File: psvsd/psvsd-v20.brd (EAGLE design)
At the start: 30 x 33.2 mm, 27 parts, among them U1 GL823(A)OG, U2 74AUP1G74DC, U3 LP3996_DSC_10

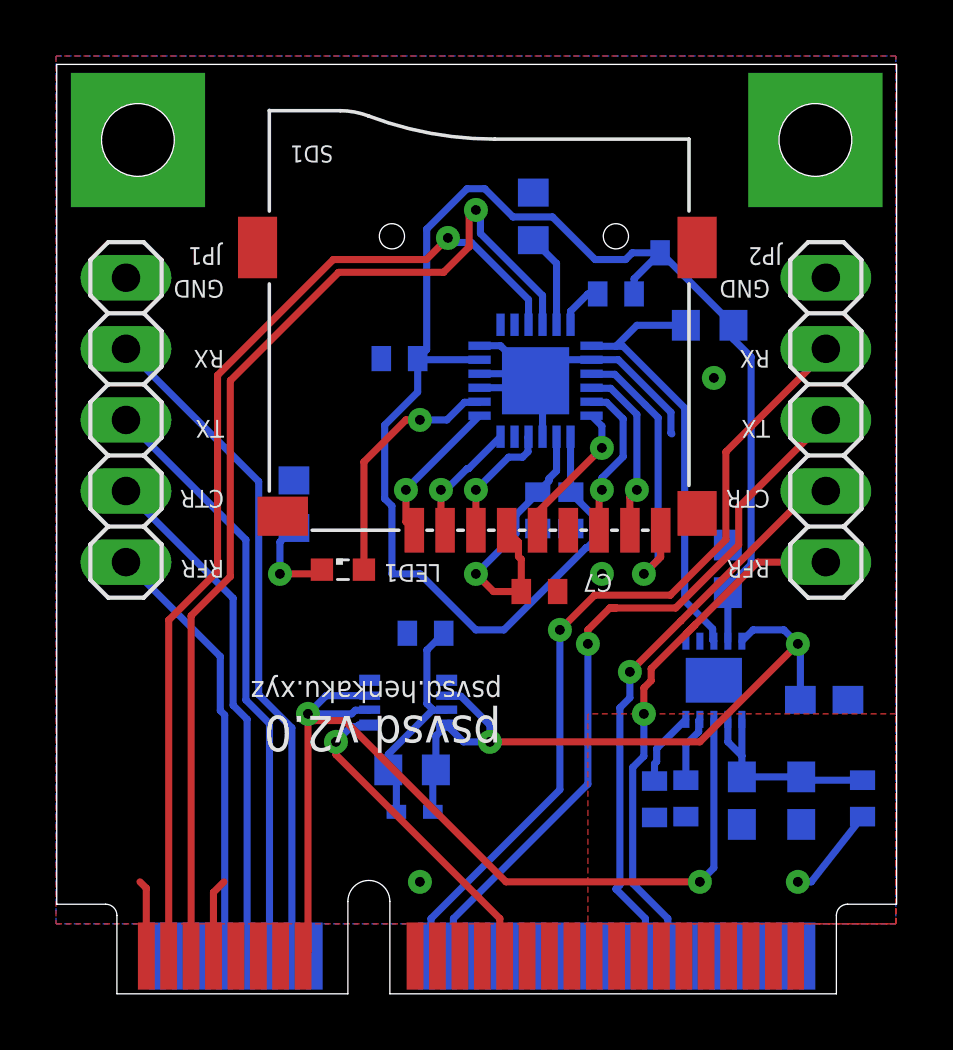
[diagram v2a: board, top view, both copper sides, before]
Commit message: Added RC delay to power circuit
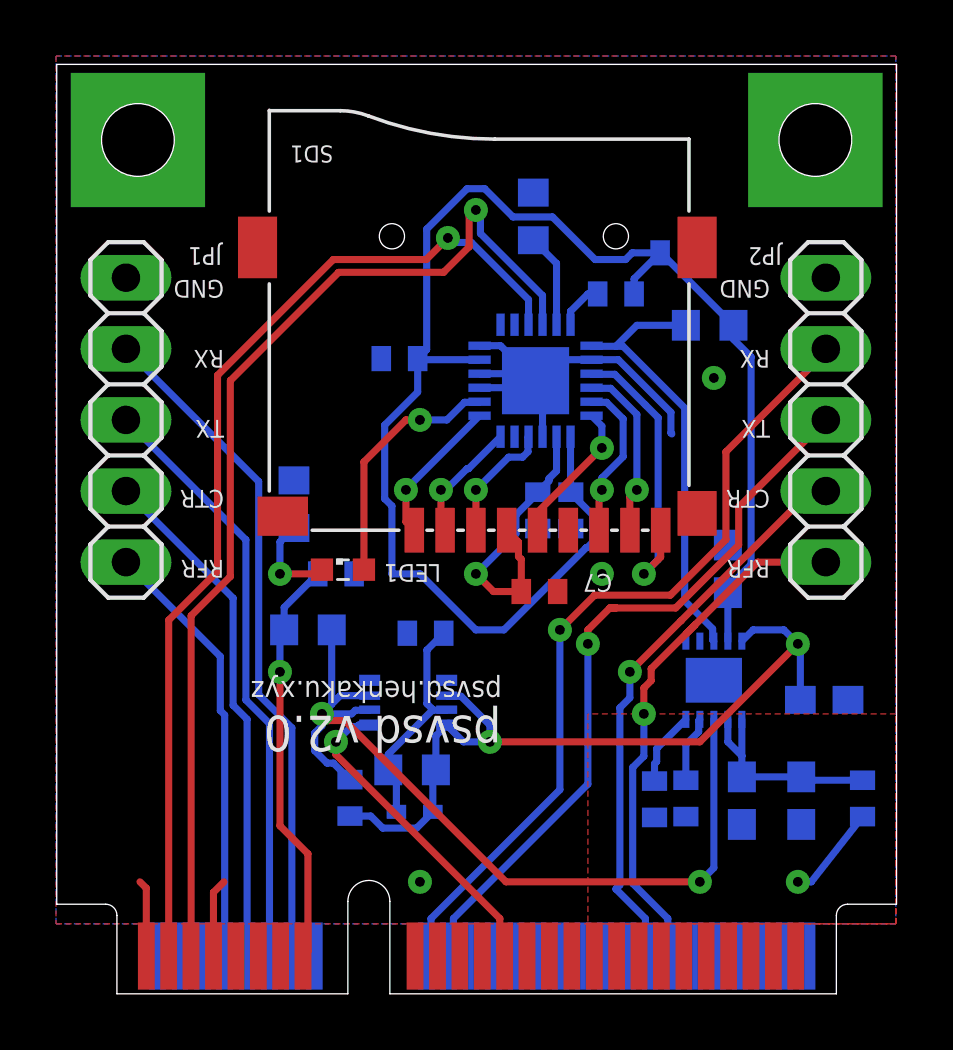
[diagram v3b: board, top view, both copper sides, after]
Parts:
- added C9: (no value), rcl:C0402
- added R4: 0, rcl:R0402
- added R5: (no value), rcl:R0603
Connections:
- new net PWR_ON: R4.2, R5.2, U2.2, U2.3, U3.3
- net GND: now also C9.2
- net PSHOLD: now also C9.1, R5.1; no longer U2.2, U2.3, U3.3
- net VDD18: now also R4.1
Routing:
- net PWR_ON: track 0.00 -> 32.0 mm, vias 0 -> 2
- net PSHOLD: track 36.0 -> 14.9 mm, vias 2 -> 1
- net VDD18: track 24.6 -> 28.0 mm
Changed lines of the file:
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@@
 <element name="SD1" library="Seeed-Connector" library_urn="urn:adsk.eagle:library:478" package="MICRO-SD9+4P-SMD-16.1X14.5X1.85MM" value="ST-TF-003A" x="15.05" y="16.56" smashed="yes" rot="R90">
 <attribute name="MPN" value="ST-TF-003A" x="15.05" y="16.56" size="1.778" layer="27" rot="R90" display="off"/>
+<attribute name="NAME" x="9.9" y="30.303" size="0.6096" layer="25" ratio="11" rot="SR180"/>
 <attribute name="NAME" x="12.891" y="21.386" size="0.254" layer="33" ratio="10" rot="R90"/>
-<attribute name="NAME" x="9.9" y="30.303" size="0.6096" layer="25" ratio="11" rot="SR180"/>
 <attribute name="VALUE" x="18.86" y="19.735" size="0.508" layer="27" ratio="10" rot="SR180"/>
 </element>
@@
 </element>
 <element name="FB2" library="inductors" library_urn="urn:adsk.eagle:library:243" package="0402" value="" x="20" y="25" rot="MR0"/>
+<element name="R4" library="rcl" library_urn="urn:adsk.eagle:library:334" package="R0402" value="0" x="10.5" y="7" rot="MR90"/>
+<element name="C9" library="rcl" library_urn="urn:adsk.eagle:library:334" package="C0402" value="" x="10" y="15" rot="MR180"/>
+<element name="R5" library="rcl" library_urn="urn:adsk.eagle:library:334" package="R0603" value="" x="9" y="13" rot="MR180"/>
 </elements>
 <signals>
@@
 <wire x1="5.626" y1="1.35" x2="5.626" y2="3.626" width="0.254" layer="1"/>
 <wire x1="5.626" y1="3.626" x2="6" y2="4" width="0.254" layer="1"/>
+<contactref element="C9" pad="2"/>
 </signal>
 <signal name="UART_KERMIT_RFR">
@@
 <wire x1="10" y1="9" x2="10" y2="8.542975" width="0.254" layer="1"/>
 <wire x1="10" y1="8.542975" x2="15.8562" y2="2.686775" width="0.254" layer="1"/>
-</signal>
-<signal name="PSHOLD">
-<contactref element="U$1" pad="15"/>
-<contactref element="U2" pad="3"/>
-<contactref element="U2" pad="2"/>
-<contactref element="U3" pad="3"/>
-<via x="23" y="4" extent="1-16" drill="0.35"/>
-<wire x1="23.5" y1="9.803" x2="23.5" y2="4.5" width="0.254" layer="16"/>
-<wire x1="23.5" y1="4.5" x2="23" y2="4" width="0.254" layer="16"/>
-<via x="9" y="10" extent="1-16" drill="0.35"/>
-<wire x1="9" y1="10" x2="9" y2="1.524" width="0.254" layer="1"/>
-<wire x1="9" y1="1.524" x2="8.826" y2="1.35" width="0.254" layer="1"/>
-<wire x1="10.563025" y1="10" x2="9" y2="10" width="0.254" layer="16"/>
-<wire x1="10.563025" y1="10" x2="10.693225" y2="10.1302" width="0.254" layer="16"/>
-<wire x1="10.693225" y1="10.1302" x2="11.1852" y2="10.1302" width="0.254" layer="16"/>
-<wire x1="11.1852" y1="10.1302" x2="11.205" y2="10.15" width="0.254" layer="16"/>
-<wire x1="9" y1="10" x2="9.65" y2="10.65" width="0.254" layer="16"/>
-<wire x1="9.65" y1="10.65" x2="11.205" y2="10.65" width="0.254" layer="16"/>
-<wire x1="9.2408" y1="9.7592" x2="9" y2="10" width="0.254" layer="1"/>
-<wire x1="10.314475" y1="9.7592" x2="9.2408" y2="9.7592" width="0.254" layer="1"/>
-<wire x1="23" y1="4" x2="16.073675" y2="4" width="0.254" layer="1"/>
-<wire x1="16.073675" y1="4" x2="10.314475" y2="9.7592" width="0.254" layer="1"/>
 </signal>
 <signal name="VDD33">
@@
 <contactref element="D1" pad="C"/>
 <contactref element="U2" pad="8"/>
-<wire x1="13.57" y1="9.215" x2="13.955" y2="9.6" width="0.254" layer="16"/>
+<wire x1="13.955" y1="9.6" x2="13.57" y2="9.215" width="0.254" layer="16"/>
 <wire x1="13.57" y1="9.215" x2="13.57" y2="8" width="0.254" layer="16"/>
 <wire x1="13.57" y1="8" x2="13.46" y2="7.89" width="0.254" layer="16"/>
-<wire x1="13.46" y1="7.89" x2="13.46" y2="6.5" width="0.254" layer="16"/>
+<wire x1="13.46" y1="6.5" x2="13.46" y2="7.89" width="0.254" layer="16"/>
 <via x="15.5" y="9" extent="1-16" drill="0.35"/>
 <via x="26.5" y="12.5" extent="1-16" drill="0.35"/>
@@
 <wire x1="26.59" y1="12.41" x2="26.59" y2="10.5" width="0.254" layer="16"/>
 <wire x1="13.955" y1="9.6" x2="14.555" y2="9" width="0.254" layer="16"/>
-<wire x1="14.555" y1="9" x2="15.5" y2="9" width="0.254" layer="16"/>
+<wire x1="15.5" y1="9" x2="14.555" y2="9" width="0.254" layer="16"/>
 <wire x1="13.955" y1="10.65" x2="13.9748" y2="10.6302" width="0.254" layer="16"/>
 <wire x1="13.9748" y1="10.6302" x2="14.466775" y2="10.6302" width="0.254" layer="16"/>
-<wire x1="14.466775" y1="10.6302" x2="15.5" y2="9.596975" width="0.254" layer="16"/>
+<wire x1="15.5" y1="9.596975" x2="14.466775" y2="10.6302" width="0.254" layer="16"/>
 <wire x1="15.5" y1="9.596975" x2="15.5" y2="9" width="0.254" layer="16"/>
 <wire x1="15.5" y1="9" x2="23" y2="9" width="0.254" layer="1"/>
 <wire x1="23" y1="9" x2="26.5" y2="12.5" width="0.254" layer="1"/>
+<contactref element="R4" pad="1"/>
+<wire x1="10.5" y1="6.35" x2="11.243025" y2="6.35" width="0.254" layer="16"/>
+<wire x1="11.243025" y1="6.35" x2="11.673225" y2="5.9198" width="0.254" layer="16"/>
+<wire x1="11.673225" y1="5.9198" x2="12.8798" y2="5.9198" width="0.254" layer="16"/>
+<wire x1="12.8798" y1="5.9198" x2="13.46" y2="6.5" width="0.254" layer="16"/>
 </signal>
 <signal name="CBYP">
@@
 <wire x1="19" y1="25" x2="19.35" y2="25" width="0.254" layer="16"/>
 </signal>
+<signal name="PWR_ON">
+<contactref element="U2" pad="3"/>
+<contactref element="U2" pad="2"/>
+<contactref element="R5" pad="2"/>
+<contactref element="U3" pad="3"/>
+<via x="23" y="4" extent="1-16" drill="0.35"/>
+<wire x1="23.5" y1="9.803" x2="23.5" y2="4.5" width="0.254" layer="16"/>
+<wire x1="23.5" y1="4.5" x2="23" y2="4" width="0.254" layer="16"/>
+<via x="9.5" y="10" extent="1-16" drill="0.35"/>
+<wire x1="23" y1="4" x2="16.073675" y2="4" width="0.254" layer="1"/>
+<contactref element="R4" pad="2"/>
+<wire x1="10.314475" y1="9.7592" x2="9.7408" y2="9.7592" width="0.254" layer="1"/>
+<wire x1="9.7408" y1="9.7592" x2="9.5" y2="10" width="0.254" layer="1"/>
+<wire x1="16.073675" y1="4" x2="10.314475" y2="9.7592" width="0.254" layer="1"/>
+<wire x1="10.563025" y1="10" x2="9.5" y2="10" width="0.254" layer="16"/>
+<wire x1="10.693225" y1="10.1302" x2="11.1852" y2="10.1302" width="0.254" layer="16"/>
+<wire x1="11.1852" y1="10.1302" x2="11.205" y2="10.15" width="0.254" layer="16"/>
+<wire x1="10.563025" y1="10" x2="10.693225" y2="10.1302" width="0.254" layer="16"/>
+<wire x1="9.5" y1="10" x2="10.15" y2="10.65" width="0.254" layer="16"/>
+<wire x1="10.15" y1="10.65" x2="11.205" y2="10.65" width="0.254" layer="16"/>
+<wire x1="9.5" y1="10" x2="9.85" y2="10.35" width="0.254" layer="16"/>
+<wire x1="9.85" y1="10.35" x2="9.85" y2="13" width="0.254" layer="16"/>
+<wire x1="9.2408" y1="9.314475" x2="9.2408" y2="8.685525" width="0.254" layer="16"/>
+<wire x1="9.2408" y1="8.685525" x2="9.685525" y2="8.2408" width="0.254" layer="16"/>
+<wire x1="9.5" y1="10" x2="9.5" y2="9.573675" width="0.254" layer="16"/>
+<wire x1="9.5" y1="9.573675" x2="9.2408" y2="9.314475" width="0.254" layer="16"/>
+<wire x1="9.685525" y1="8.2408" x2="9.9092" y2="8.2408" width="0.254" layer="16"/>
+<wire x1="9.9092" y1="8.2408" x2="10.5" y2="7.65" width="0.254" layer="16"/>
+</signal>
+<signal name="PSHOLD">
+<contactref element="U$1" pad="15"/>
+<contactref element="R5" pad="1"/>
+<contactref element="C9" pad="1"/>
+<via x="8" y="11.5" extent="1-16" drill="0.35"/>
+<wire x1="8.15" y1="13.8" x2="8.15" y2="13" width="0.254" layer="16"/>
+<wire x1="8.15" y1="13.8" x2="9.35" y2="15" width="0.254" layer="16"/>
+<wire x1="8.15" y1="13" x2="8" y2="12.85" width="0.254" layer="16"/>
+<wire x1="8" y1="12.85" x2="8" y2="11.5" width="0.254" layer="16"/>
+<wire x1="8.826" y1="1.35" x2="8.6562" y2="1.5198" width="0.254" layer="1"/>
+<wire x1="8" y1="11.5" x2="8" y2="6" width="0.254" layer="1"/>
+<wire x1="8" y1="6" x2="9" y2="5" width="0.254" layer="1"/>
+<wire x1="9" y1="5" x2="9" y2="1.524" width="0.254" layer="1"/>
+<wire x1="9" y1="1.524" x2="8.826" y2="1.35" width="0.254" layer="1"/>
+</signal>
 </signals>
